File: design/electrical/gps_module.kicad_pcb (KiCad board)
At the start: 2 copper layers, 90.2 x 95.9 mm, 21 parts, among them IC1 ATMEGA16M1-A, J1 SMA, U1 TPS2030, U2 LM1117-3.3, U3 RXM-GPS-RM, U4 ADG787, U5 ATA6561, U6 ATA6561

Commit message: Added decupling capacitors for CAN and MUX
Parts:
- added C3: 1uF, Capacitors_SMD:C_0805, F.Cu at (74.4, 69.8)
- added C4: 1uF, Capacitors_SMD:C_0805, F.Cu at (86.6, 74.9)
- added C5: 1uF, Capacitors_SMD:C_0805, F.Cu at (70.7, 77.1)
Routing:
- net GND: track 148.9 -> 174.2 mm, vias 8 -> 11
- net (no net): track 2.76 -> 0.00 mm, vias 2 -> 0
- net CAN_SEL: track 43.6 -> 44.4 mm

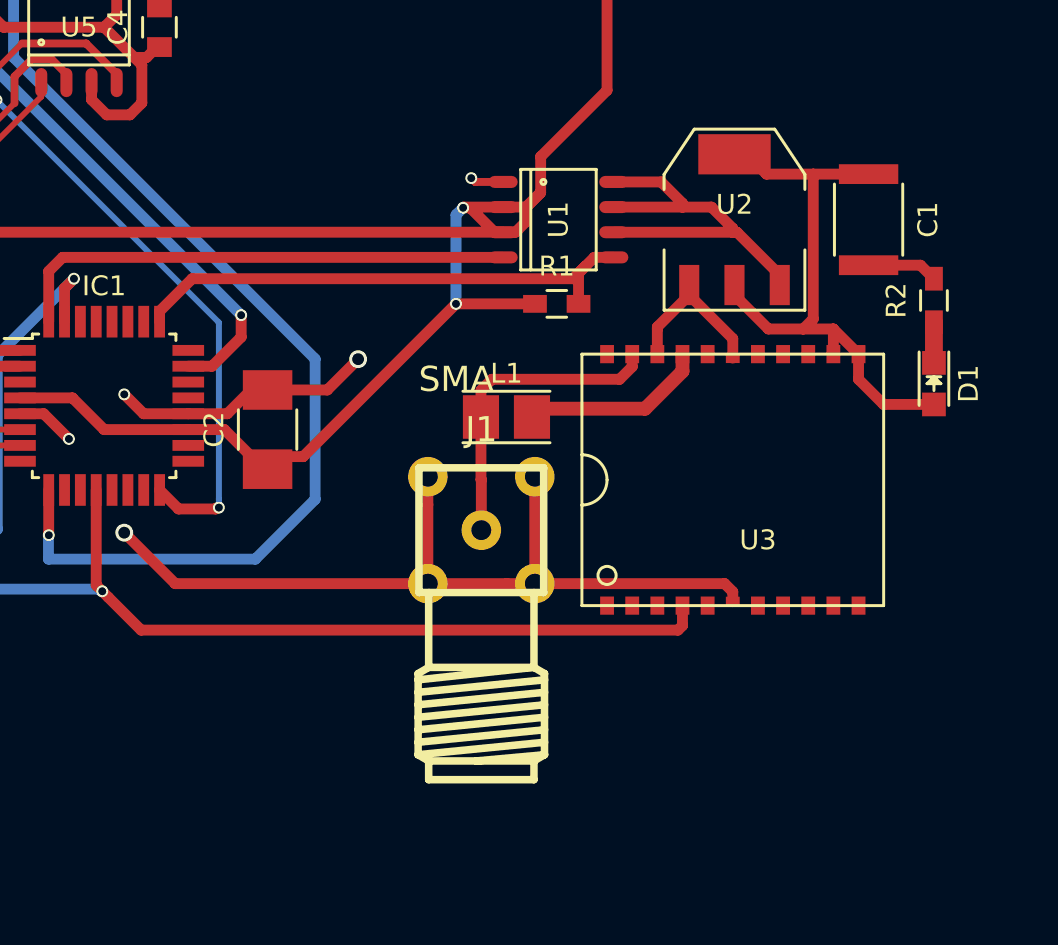
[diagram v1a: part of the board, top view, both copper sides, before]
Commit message: Rotated GPS module, increased GPS antenna track width
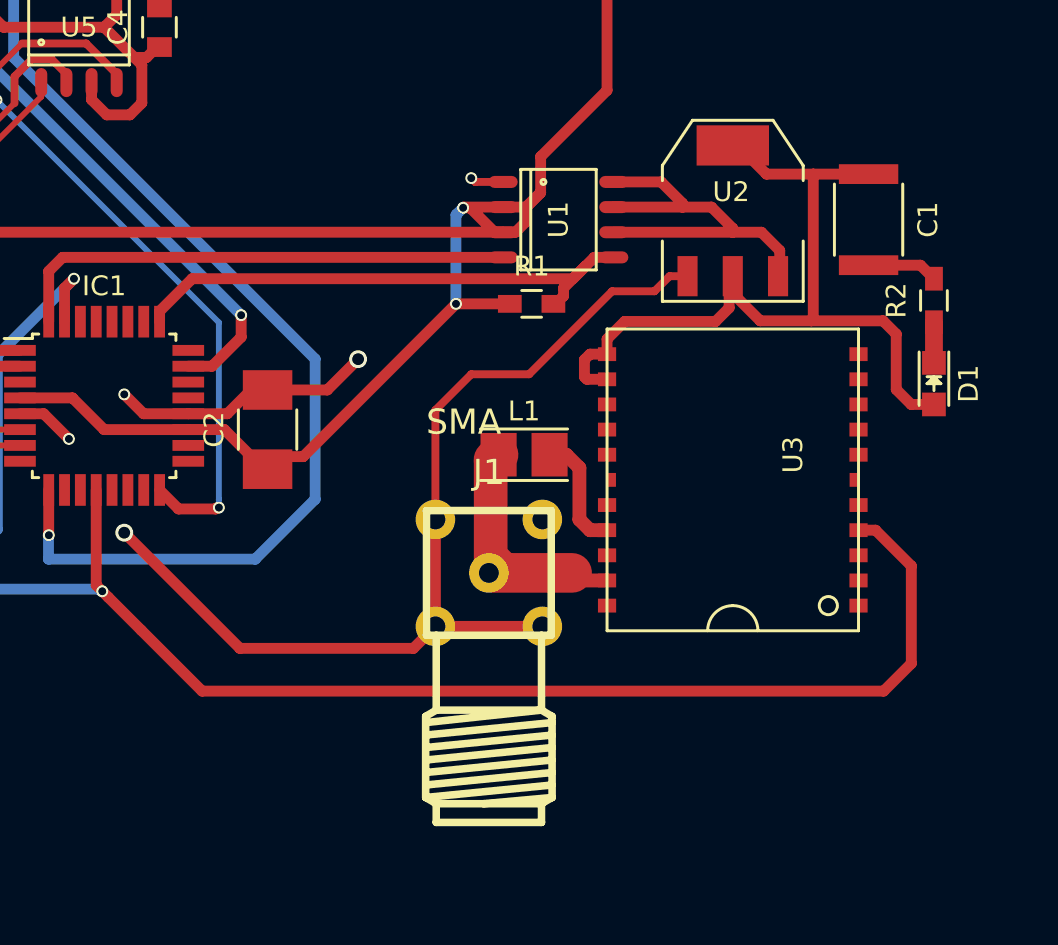
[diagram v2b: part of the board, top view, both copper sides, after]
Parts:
- moved J1 2.19 mm to (103.3, 102.5)
- moved L1 2.10 mm to (105.0, 96.5)
- moved R1 1.27 mm to (105.4, 88.9)
- moved U2 0.45 mm to (115.6, 84.2)
- turned U3 to 90 degrees
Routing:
- net GPS_TX: track 60.0 -> 80.7 mm
- net Net-(C1-Pad1): track 29.7 -> 41.3 mm
- net Net-(J1-Pad1): track 15.8 -> 12.3 mm
- net Net-(L1-Pad2): track 9.43 -> 6.01 mm
- net +5V: track 162.0 -> 160.8 mm
- net GND: track 174.2 -> 173.1 mm
- net Net-(U1-Pad6): track 20.5 -> 21.3 mm

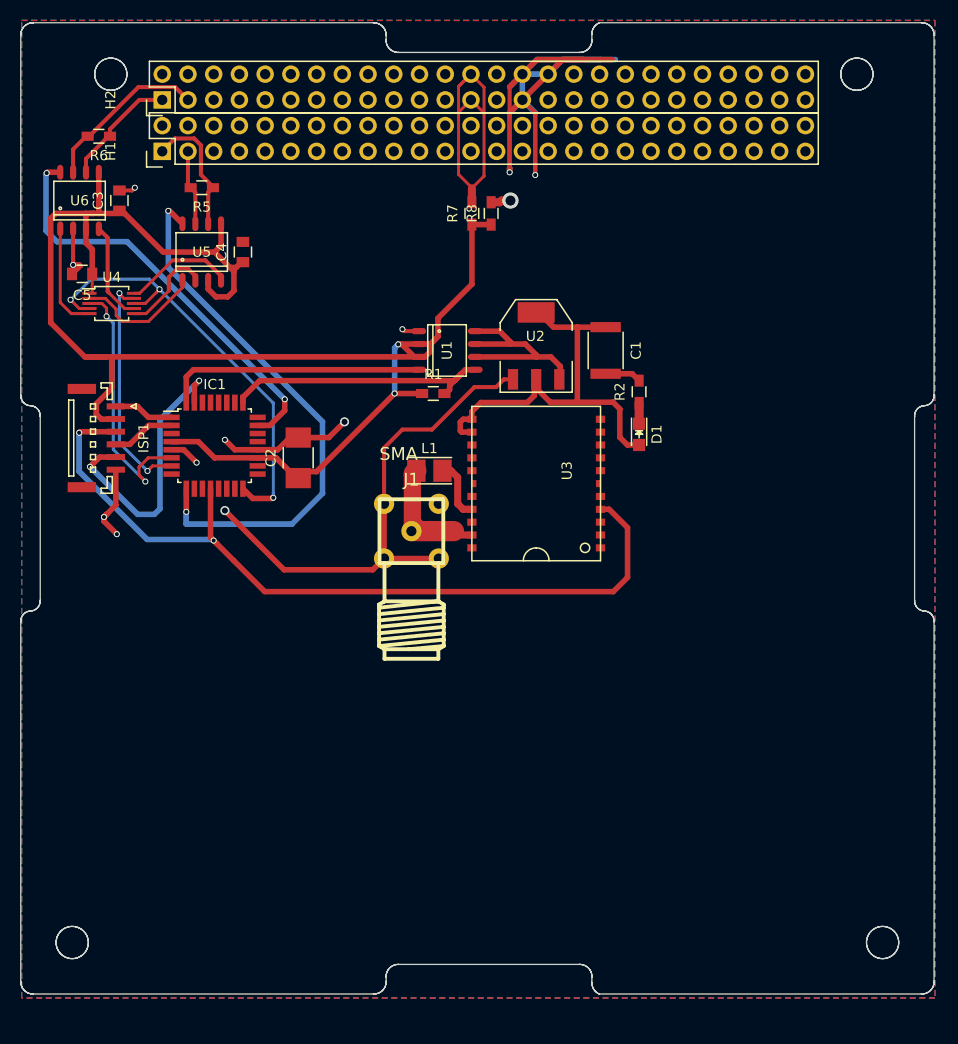
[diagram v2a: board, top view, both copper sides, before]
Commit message: Changed IC to 3.3V, added 1 LDO, 2 Leds, 1uart port, changed footprints to 0603, updated layout.
Still 2 unconnected traces reported by Kicad.
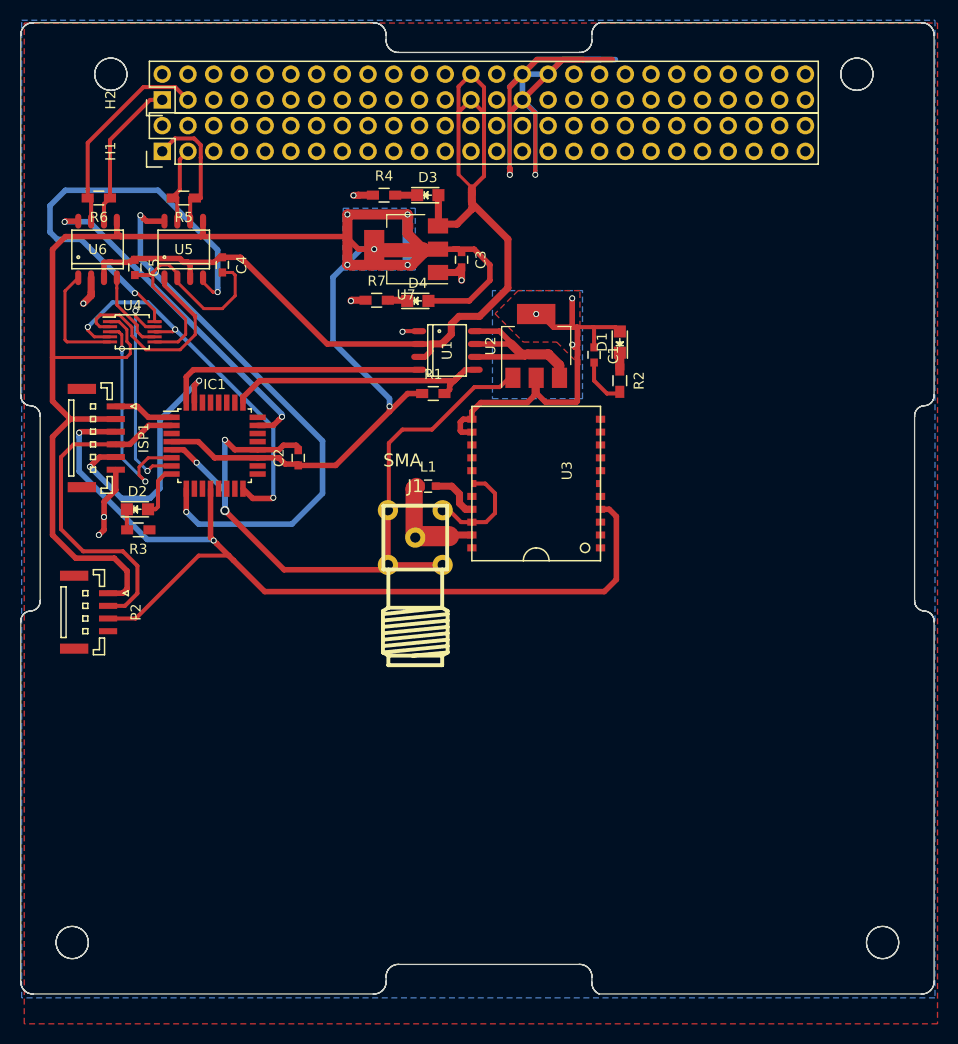
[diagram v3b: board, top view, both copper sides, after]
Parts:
- removed R8: DNP, Resistors_SMD:R_0603_HandSoldering
- added D2: Led_Small, LEDs:LED_0805, F.Cu at (76.2, 100.3)
- added D3: Led_Small, LEDs:LED_0805, F.Cu at (104.9, 69.3)
- added D4: Led_Small, LEDs:LED_0805, F.Cu at (103.9, 79.8)
- added P2: CONN_01X04, Connectors_JST:JST_GH_BM04B-GHS-TBT_04x1.25mm_Straight, F.Cu at (71.6, 110.5)
- added R3: 1k, Resistors_SMD:R_0603_HandSoldering, F.Cu at (76.3, 102.4)
- added R4: 1k, Resistors_SMD:R_0603_HandSoldering, F.Cu at (100.6, 69.3)
- added U7: LM1117-3.3, TO_SOT_Packages_SMD:SOT-223, F.Cu at (102.7, 74.7)
- C1: footprint Capacitors_SMD:C_1812 -> Capacitors_SMD:C_0603
- C2: footprint Capacitors_SMD:C_1210_HandSoldering -> Capacitors_SMD:C_0603
- C3, C4, C5: footprint Capacitors_SMD:C_0805 -> Capacitors_SMD:C_0603
- L1: footprint Inductors:Inductor_Taiyo-Yuden_NR-24xx_HandSoldering -> Capacitors_SMD:C_0603
- R7: value 0 -> 1k
- moved C3 34.3 mm to (108.2, 75.7), turned to 270 degrees
- moved R7 12.7 mm to (99.8, 79.7), turned to 0 degrees
- moved D1 9.31 mm to (123.8, 83.8), turned to 90 degrees
- moved R6 6.10 mm to (72.4, 69.6)
- moved C5 5.25 mm to (75.9, 76.5), turned to 270 degrees
- moved U6 5.14 mm to (72.3, 74.7)
- moved U4 3.45 mm to (75.7, 82.8)
- moved C4 2.40 mm to (84.6, 76.2), turned to 270 degrees
- moved R2 2.20 mm to (123.8, 87.6), turned to 270 degrees
- moved R5 2.05 mm to (80.8, 69.6)
- moved U5 1.80 mm to (80.8, 74.7)
- moved L1 1.53 mm to (104.9, 98.0)
- moved C1 1.23 mm to (121.3, 85.1)
- moved J1 0.74 mm to (103.6, 103.1)
- turned U2 to 90 degrees
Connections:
- net Net-(C1-Pad1) renamed /3V3_GPS
- C2 pad 1: +5V -> +3V3
- C3 pad 1: +5V -> +3V3
- C4 pad 1: +5V -> 5V_BUS
- C5 pad 1: +5V -> 5V_BUS
- IC1 pad 19: +5V -> +3V3
- IC1 pad 4: +5V -> +3V3
- ISP1 pad 2: +5V -> +3V3
- R1 pad 1: +5V -> +3V3
- R7 pad 1: +5V -> GND
- R7 pad 2: 5V_BUS -> Net-(D4-Pad1)
- U1 pad 2: +5V -> 5V_BUS
- U1 pad 3: +5V -> 5V_BUS
- U4 pad 1: +5V -> +3V3
- U5 pad 3: +5V -> 5V_BUS
- U5 pad 5: +5V -> +3V3
- U6 pad 3: +5V -> 5V_BUS
- U6 pad 5: +5V -> +3V3
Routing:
- net +3V3: track 0.00 -> 194.9 mm, vias 0 -> 6
- net +5V: track 160.8 -> 0.00 mm, vias 2 -> 0
- net 5V_BUS: track 32.9 -> 103.8 mm
- net GND: track 173.1 -> 212.1 mm, vias 11 -> 12
- net Net-(U4-Pad10): track 11.0 -> 44.3 mm, vias 0 -> 2
- net Net-(IC1-Pad2): track 6.88 -> 35.1 mm
- net GPS_TX: track 80.7 -> 93.7 mm
- net CAN2_STBY: track 42.0 -> 33.7 mm
- net Net-(U4-Pad2): track 13.0 -> 21.3 mm
- net Net-(D2-Pad2): track 0.00 -> 5.25 mm
- net CAN_SEL: track 44.4 -> 40.1 mm
- net CAN2_H: track 16.7 -> 20.7 mm
- net TX_CAN: track 25.9 -> 22.0 mm
- net CAN2_L: track 11.7 -> 15.1 mm
- net Net-(IC1-Pad31): track 28.7 -> 26.2 mm
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- added copper zone on B.Cu, net +3V3
- added copper zone on F.Cu, net +3V3
- added copper zone on B.Cu, net /3V3_GPS
- added copper zone on F.Cu, net /3V3_GPS
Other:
- net class Default: trace_width 0.4 -> 0.7

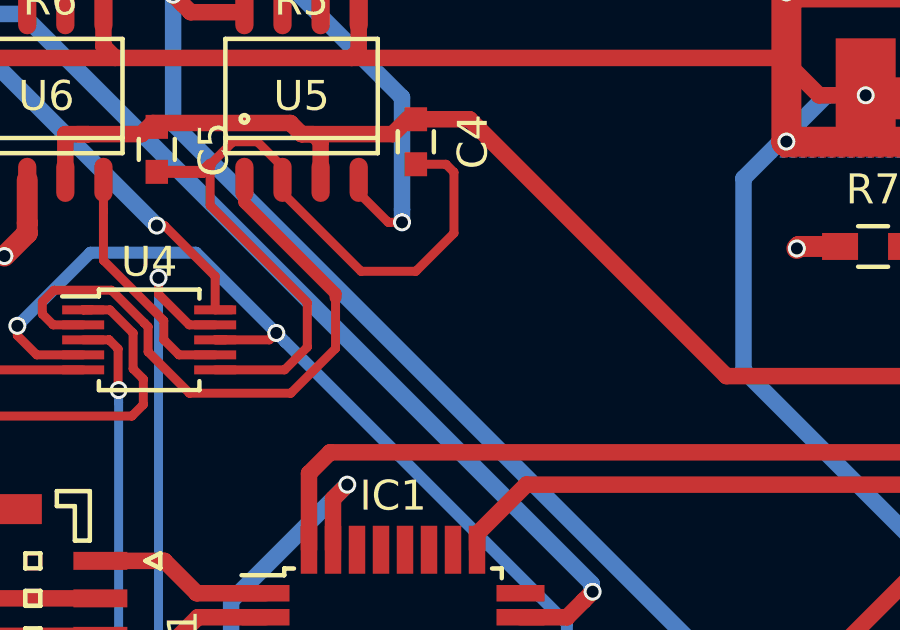
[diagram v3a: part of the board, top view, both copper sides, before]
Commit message: fix unconnected track
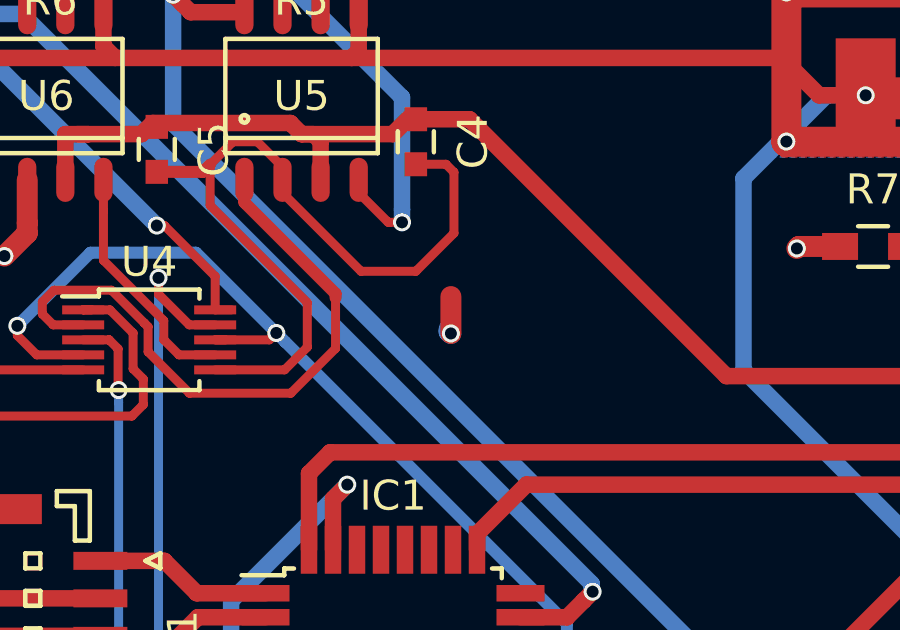
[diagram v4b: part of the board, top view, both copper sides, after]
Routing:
- net GND: track 212.1 -> 213.5 mm, vias 12 -> 13
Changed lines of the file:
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@@
   (general
     (links 94)
-    (no_connects 1)
-    (area 64.631099 52.243599 154.901101 148.233601)
+    (no_connects 0)
+    (area 64.631099 52.047565 155.194001 151.130001)
     (thickness 1.6)
     (drawings 1584)
-    (tracks 536)
+    (tracks 540)
     (zones 0)
     (modules 30)
@@
   (layers
     (0 F.Cu signal)
-    (31 B.Cu signal)
+    (31 B.Cu signal hide)
     (32 B.Adhes user)
     (33 F.Adhes user)
@@
   (gr_line (start 64.682402 146.9336) (end 64.681359 146.95864) (layer Edge.Cuts) (width 0.1))
   (gr_line (start 64.6811 146.9336) (end 64.682402 146.9336) (layer Edge.Cuts) (width 0.1))
+  (segment (start 85.75 81.36) (end 85.75 82.59) (width 0.7) (layer F.Cu) (net 1))
+  (segment (start 85.69 82.53) (end 85.69 82.45) (width 0.7) (layer B.Cu) (net 1))
+  (segment (start 85.75 82.59) (end 85.69 82.53) (width 0.7) (layer B.Cu) (net 1))
+  (via (at 85.75 82.59) (size 0.6) (drill 0.4) (layers F.Cu B.Cu) (net 1))
   (segment (start 98.722 79.690637) (end 97.347363 79.690637) (width 0.7) (layer F.Cu) (net 1))
   (segment (start 97.347363 79.690637) (end 97.282 79.756) (width 0.7) (layer F.Cu) (net 1))
